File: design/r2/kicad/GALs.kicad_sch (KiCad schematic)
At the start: 12 parts, among them IC2 ATF22V10C, IC3 ATF22V10C, IC5 ATF22V10C, IC6 ATF22V10C

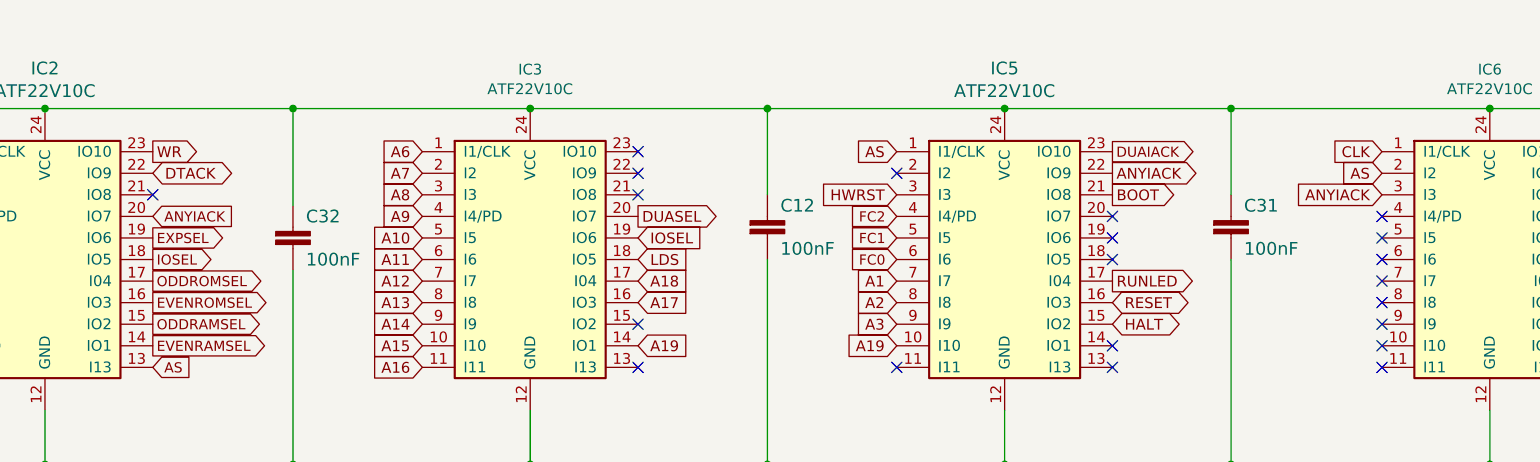
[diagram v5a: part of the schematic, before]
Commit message: Update designs for copro GAL change
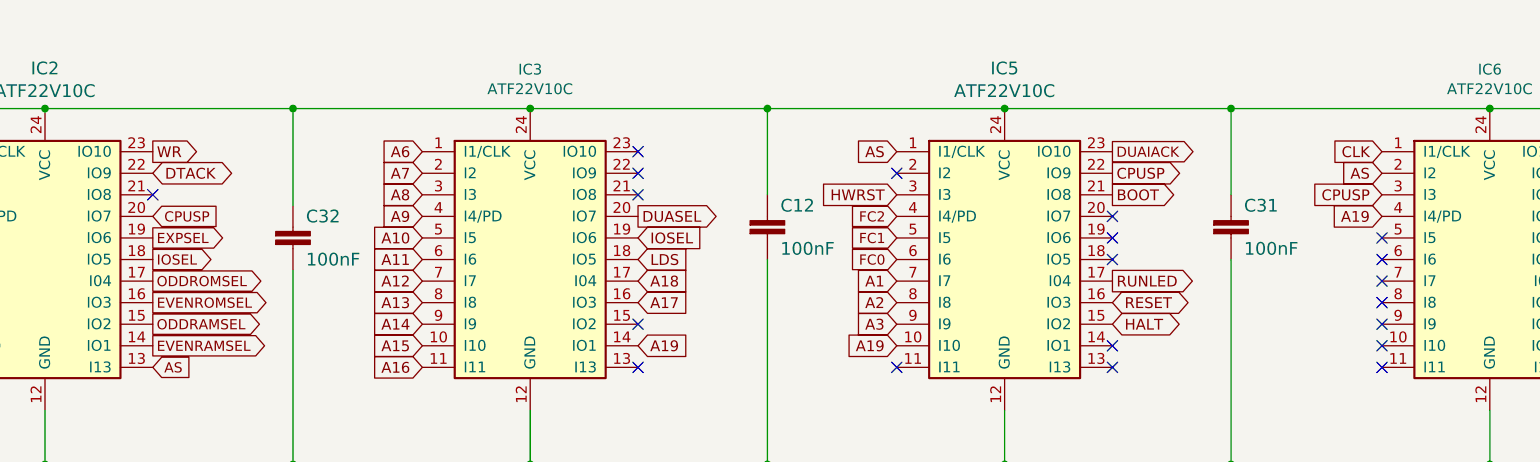
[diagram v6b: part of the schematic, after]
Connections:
- net A19: now also IC6.4 (I4/PD)
- net ANYIACK renamed CPUSP
- no-connect marks 30 -> 29
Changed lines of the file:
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@@
   (title_block
     (title "ROSCO_M68K GENERAL PURPOSE MC68010 COMPUTER")
-    (date "2024-03-09")
+    (date "2024-03-17")
     (rev "2.2")
     (company "The Really Old-School Company Limited")
@@
   )
   (no_connect (at 133.35 88.9))
-  (no_connect (at 220.98 93.98))
   (no_connect (at 133.35 91.44))
   (no_connect (at 133.35 106.68))
@@
     )
   )
+  (global_label "A19" (shape input) (at 220.98 93.98 180) (fields_autoplaced)
+    (effects (font (size 1.27 1.27)) (justify right))
+    (property "Intersheetrefs" "${INTERSHEET_REFS}" (at 215.1414 93.98 0)
+      (effects (font (size 1.27 1.27)) (justify right) hide)
+    )
+  )
   (global_label "A3" (shape input) (at 163.83 106.68 180) (fields_autoplaced)
     (effects (font (size 1.27 1.27)) (justify right))
@@
     )
   )
-  (global_label "ANYIACK" (shape input) (at 220.98 91.44 180) (fields_autoplaced)
-    (effects (font (size 1.27 1.27)) (justify right))
-    (property "Intersheetrefs" "${INTERSHEET_REFS}" (at 0 0 0)
-      (effects (font (size 1.27 1.27)) hide)
+  (global_label "CPUSP" (shape input) (at 220.98 91.44 180) (fields_autoplaced)
+    (effects (font (size 1.27 1.27)) (justify right))
+    (property "Intersheetrefs" "${INTERSHEET_REFS}" (at 212.299 91.44 0)
+      (effects (font (size 1.27 1.27)) (justify right) hide)
     )
   )
@@
     )
   )
-  (global_label "ANYIACK" (shape input) (at 76.2 93.98 0) (fields_autoplaced)
+  (global_label "CPUSP" (shape input) (at 76.2 93.98 0) (fields_autoplaced)
     (effects (font (size 1.1938 1.1938)) (justify left))
-    (property "Intersheetrefs" "${INTERSHEET_REFS}" (at 0 0 0)
-      (effects (font (size 1.27 1.27)) hide)
+    (property "Intersheetrefs" "${INTERSHEET_REFS}" (at 84.3599 93.98 0)
+      (effects (font (size 1.27 1.27)) (justify left) hide)
     )
   )
@@
     )
   )
-  (global_label "ANYIACK" (shape output) (at 189.23 88.9 0) (fields_autoplaced)
-    (effects (font (size 1.27 1.27)) (justify left))
-    (property "Intersheetrefs" "${INTERSHEET_REFS}" (at 0 0 0)
-      (effects (font (size 1.27 1.27)) hide)
-    )
-  )
+  (global_label "CPUSP" (shape output) (at 189.23 88.9 0) (fields_autoplaced)
+    (effects (font (size 1.27 1.27)) (justify left))
+    (property "Intersheetrefs" "${INTERSHEET_REFS}" (at 197.911 88.9 0)
+      (effects (font (size 1.27 1.27)) (justify left) hide)
+    )
+  )

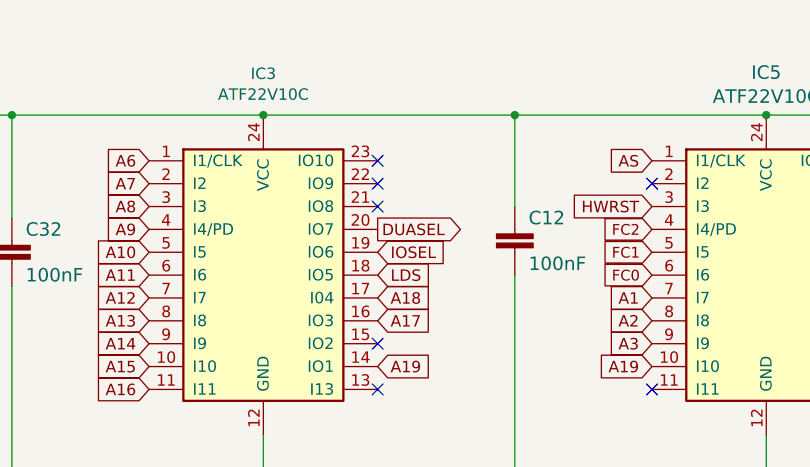
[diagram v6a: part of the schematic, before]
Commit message: Tentative r2 SMD design
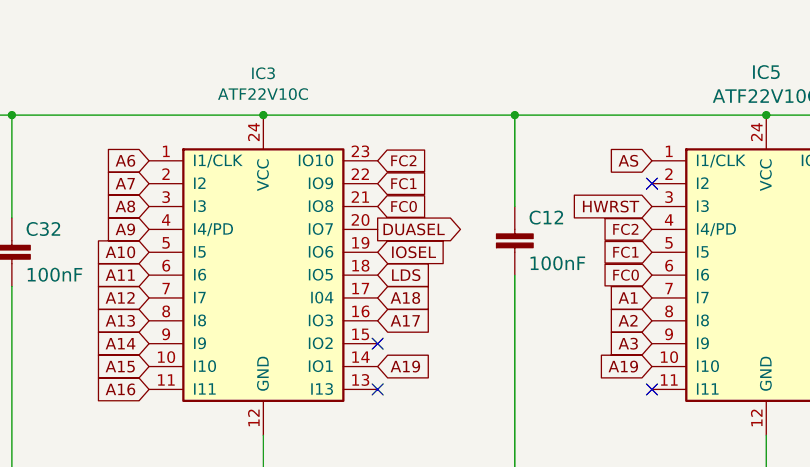
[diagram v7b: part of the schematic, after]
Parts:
- C10, C12, C31, C32, C9: footprint rosco_m68k:C2.5-3 -> Capacitor_SMD:C_0603_1608Metric
- R21, R8: footprint rosco_m68k:0207_10 -> Resistor_SMD:R_0603_1608Metric
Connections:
- net FC0: now also IC3.21 (IO8)
- net FC1: now also IC3.22 (IO9)
- net FC2: now also IC3.23 (IO10)
- no-connect marks 29 -> 26
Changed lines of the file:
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@@
   (junction (at 55.88 177.8) (diameter 0) (color 0 0 0 0)
   )
-  (no_connect (at 133.35 88.9))
-  (no_connect (at 133.35 91.44))
   (no_connect (at 133.35 106.68))
-  (no_connect (at 133.35 86.36))
   (no_connect (at 246.38 99.06))
   (no_connect (at 246.38 93.98))
@@
     )
   )
+  (global_label "FC1" (shape input) (at 133.35 88.9 0) (fields_autoplaced)
+    (effects (font (size 1.1938 1.1938)) (justify left))
+    (property "Intersheetrefs" "${INTERSHEET_REFS}" (at 138.895 88.9 0)
+      (effects (font (size 1.27 1.27)) (justify left) hide)
+    )
+  )
   (global_label "HWRST" (shape input) (at 163.83 91.44 180) (fields_autoplaced)
     (effects (font (size 1.27 1.27)) (justify right))
@@
     (property "Intersheetrefs" "${INTERSHEET_REFS}" (at 0 0 0)
       (effects (font (size 1.27 1.27)) hide)
+    )
+  )
+  (global_label "FC2" (shape input) (at 133.35 86.36 0) (fields_autoplaced)
+    (effects (font (size 1.1938 1.1938)) (justify left))
+    (property "Intersheetrefs" "${INTERSHEET_REFS}" (at 138.895 86.36 0)
+      (effects (font (size 1.27 1.27)) (justify left) hide)
     )
   )
@@
     (property "Intersheetrefs" "${INTERSHEET_REFS}" (at 0 0 0)
       (effects (font (size 1.27 1.27)) hide)
+    )
+  )
+  (global_label "FC0" (shape input) (at 133.35 91.44 0) (fields_autoplaced)
+    (effects (font (size 1.1938 1.1938)) (justify left))
+    (property "Intersheetrefs" "${INTERSHEET_REFS}" (at 138.895 91.44 0)
+      (effects (font (size 1.27 1.27)) (justify left) hide)
     )
   )
@@
       (effects (font (size 1.4986 1.4986)) (justify left bottom))
     )
-    (property "Footprint" "rosco_m68k:C2.5-3" (at 35.56 95.25 0)
+    (property "Footprint" "Capacitor_SMD:C_0603_1608Metric" (at 35.56 95.25 0)
       (effects (font (size 1.27 1.27)) hide)
     )
@@
       (effects (font (size 1.4986 1.4986)) (justify left bottom))
     )
-    (property "Footprint" "rosco_m68k:C2.5-3" (at 148.59 93.98 0)
+    (property "Footprint" "Capacitor_SMD:C_0603_1608Metric" (at 148.59 93.98 0)
       (effects (font (size 1.27 1.27)) hide)
     )
@@
       (effects (font (size 1.27 1.27)) (justify left))
     )
-    (property "Footprint" "rosco_m68k:0207_10" (at 54.102 157.48 90)
+    (property "Footprint" "Resistor_SMD:R_0603_1608Metric" (at 54.102 157.48 90)
       (effects (font (size 1.27 1.27)) hide)
     )
@@
       (effects (font (size 1.27 1.27)) (justify left))
     )
-    (property "Footprint" "rosco_m68k:0207_10" (at 62.992 157.48 90)
+    (property "Footprint" "Resistor_SMD:R_0603_1608Metric" (at 62.992 157.48 90)
       (effects (font (size 1.27 1.27)) hide)
     )
@@
       (effects (font (size 1.4986 1.4986)) (justify left bottom))
     )
-    (property "Footprint" "rosco_m68k:C2.5-3" (at 261.62 93.98 0)
+    (property "Footprint" "Capacitor_SMD:C_0603_1608Metric" (at 261.62 93.98 0)
       (effects (font (size 1.27 1.27)) hide)
     )
@@
       (effects (font (size 1.4986 1.4986)) (justify left bottom))
     )
-    (property "Footprint" "rosco_m68k:C2.5-3" (at 203.2 93.98 0)
+    (property "Footprint" "Capacitor_SMD:C_0603_1608Metric" (at 203.2 93.98 0)
       (effects (font (size 1.27 1.27)) hide)
     )
@@
       (effects (font (size 1.4986 1.4986)) (justify left bottom))
     )
-    (property "Footprint" "rosco_m68k:C2.5-3" (at 92.71 95.25 0)
-      (effects (font (size 1.27 1.27)) hide)
-    )
+    (property "Footprint" "Capacitor_SMD:C_0603_1608Metric" (at 92.71 95.25 0)
+      (effects (font (size 1.27 1.27)) hide)
+    )

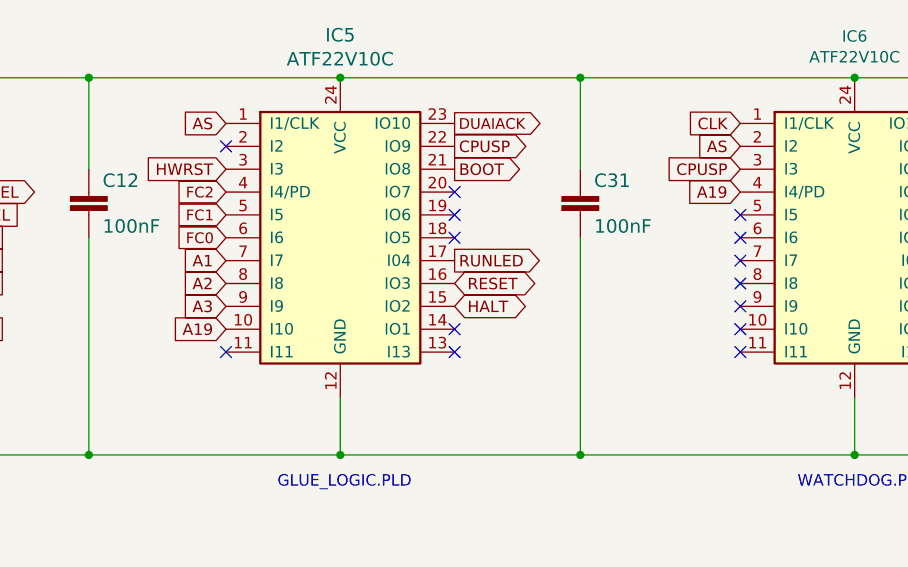
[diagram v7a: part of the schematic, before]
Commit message: More address lines into GALs
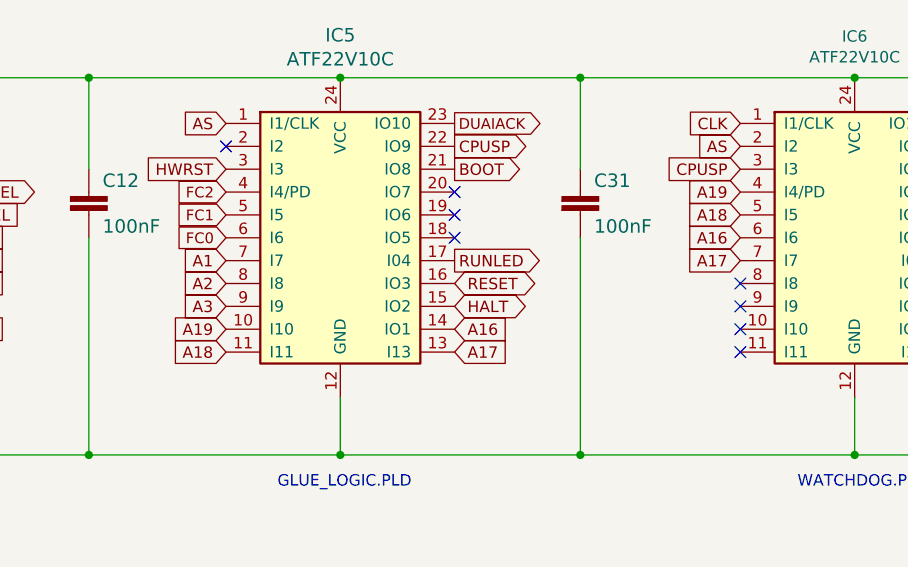
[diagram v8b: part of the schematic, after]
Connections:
- net A16: now also IC5.14 (IO1), IC6.6 (I6)
- net A17: now also IC5.13 (I13), IC6.7 (I7)
- net A18: now also IC5.11 (I11), IC6.5 (I5)
- no-connect marks 26 -> 20
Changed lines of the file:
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@@
   (no_connect (at 246.38 93.98))
   (no_connect (at 220.98 111.76))
-  (no_connect (at 220.98 101.6))
   (no_connect (at 246.38 91.44))
-  (no_connect (at 189.23 111.76))
   (no_connect (at 246.38 109.22))
-  (no_connect (at 220.98 99.06))
   (no_connect (at 76.2 91.44))
   (no_connect (at 133.35 111.76))
@@
   (no_connect (at 246.38 96.52))
   (no_connect (at 189.23 96.52))
-  (no_connect (at 220.98 96.52))
-  (no_connect (at 163.83 111.76))
   (no_connect (at 246.38 106.68))
   (no_connect (at 246.38 104.14))
   (no_connect (at 246.38 101.6))
-  (no_connect (at 189.23 109.22))
   (no_connect (at 220.98 109.22))
   (no_connect (at 220.98 104.14))
@@
     )
   )
+  (global_label "A16" (shape input) (at 189.23 109.22 0) (fields_autoplaced)
+    (effects (font (size 1.27 1.27)) (justify left))
+    (property "Intersheetrefs" "${INTERSHEET_REFS}" (at 195.0686 109.22 0)
+      (effects (font (size 1.27 1.27)) (justify left) hide)
+    )
+  )
   (global_label "A3" (shape input) (at 163.83 106.68 180) (fields_autoplaced)
     (effects (font (size 1.27 1.27)) (justify right))
@@
     )
   )
+  (global_label "A16" (shape input) (at 220.98 99.06 180) (fields_autoplaced)
+    (effects (font (size 1.27 1.27)) (justify right))
+    (property "Intersheetrefs" "${INTERSHEET_REFS}" (at 215.1414 99.06 0)
+      (effects (font (size 1.27 1.27)) (justify right) hide)
+    )
+  )
   (global_label "WR" (shape output) (at 76.2 86.36 0) (fields_autoplaced)
     (effects (font (size 1.27 1.27)) (justify left))
@@
     )
   )
+  (global_label "A18" (shape input) (at 220.98 96.52 180) (fields_autoplaced)
+    (effects (font (size 1.27 1.27)) (justify right))
+    (property "Intersheetrefs" "${INTERSHEET_REFS}" (at 215.1414 96.52 0)
+      (effects (font (size 1.27 1.27)) (justify right) hide)
+    )
+  )
   (global_label "FC2" (shape input) (at 133.35 86.36 0) (fields_autoplaced)
     (effects (font (size 1.1938 1.1938)) (justify left))
@@
     )
   )
+  (global_label "A17" (shape input) (at 189.23 111.76 0) (fields_autoplaced)
+    (effects (font (size 1.27 1.27)) (justify left))
+    (property "Intersheetrefs" "${INTERSHEET_REFS}" (at 195.0686 111.76 0)
+      (effects (font (size 1.27 1.27)) (justify left) hide)
+    )
+  )
   (global_label "LGEXP" (shape input) (at 45.72 177.8 180) (fields_autoplaced)
     (effects (font (size 1.27 1.27)) (justify right))
@@
     (property "Intersheetrefs" "${INTERSHEET_REFS}" (at 0 0 0)
       (effects (font (size 1.27 1.27)) hide)
+    )
+  )
+  (global_label "A17" (shape input) (at 220.98 101.6 180) (fields_autoplaced)
+    (effects (font (size 1.27 1.27)) (justify right))
+    (property "Intersheetrefs" "${INTERSHEET_REFS}" (at 215.1414 101.6 0)
+      (effects (font (size 1.27 1.27)) (justify right) hide)
     )
   )
@@
     )
   )
+  (global_label "A18" (shape input) (at 163.83 111.76 180) (fields_autoplaced)
+    (effects (font (size 1.27 1.27)) (justify right))
+    (property "Intersheetrefs" "${INTERSHEET_REFS}" (at 157.9914 111.76 0)
+      (effects (font (size 1.27 1.27)) (justify right) hide)
+    )
+  )
